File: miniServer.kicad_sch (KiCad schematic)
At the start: 1 part, among them U1 STM32H725VGTx

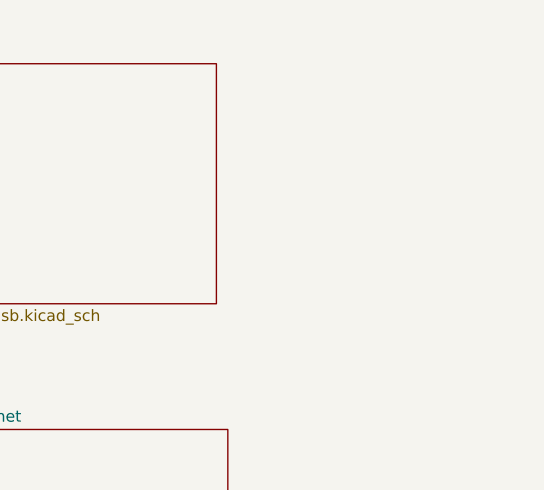
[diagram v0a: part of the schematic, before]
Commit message: Added SDMMC
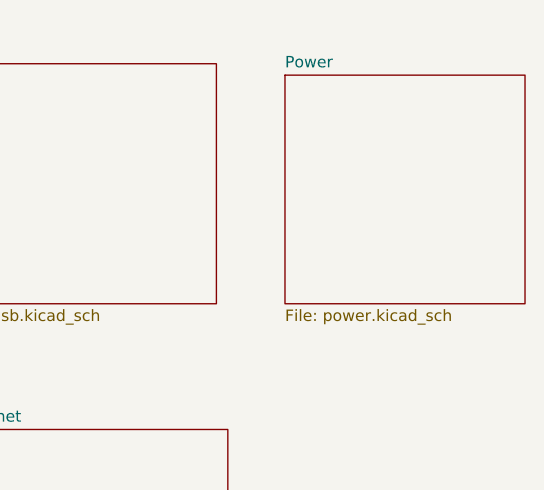
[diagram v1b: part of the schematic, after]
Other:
- added sheet Power (power.kicad_sch)

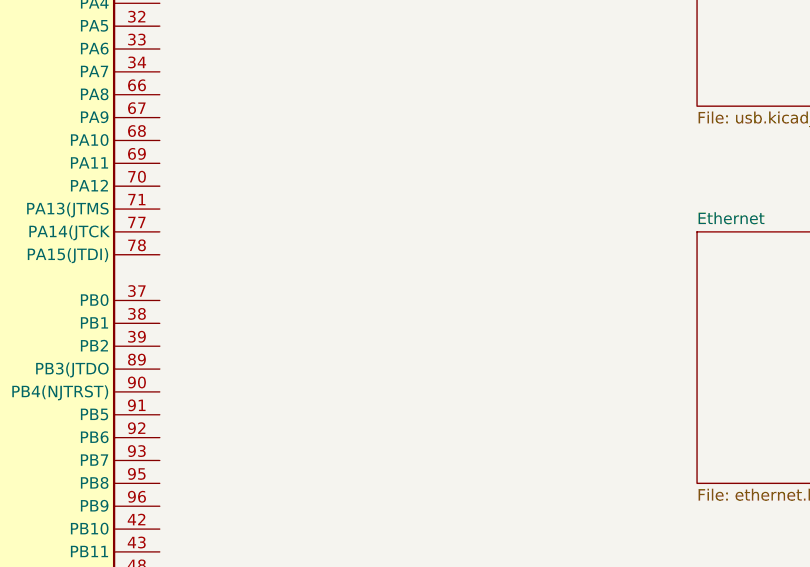
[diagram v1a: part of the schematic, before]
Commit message: Placed some components on PCB layout
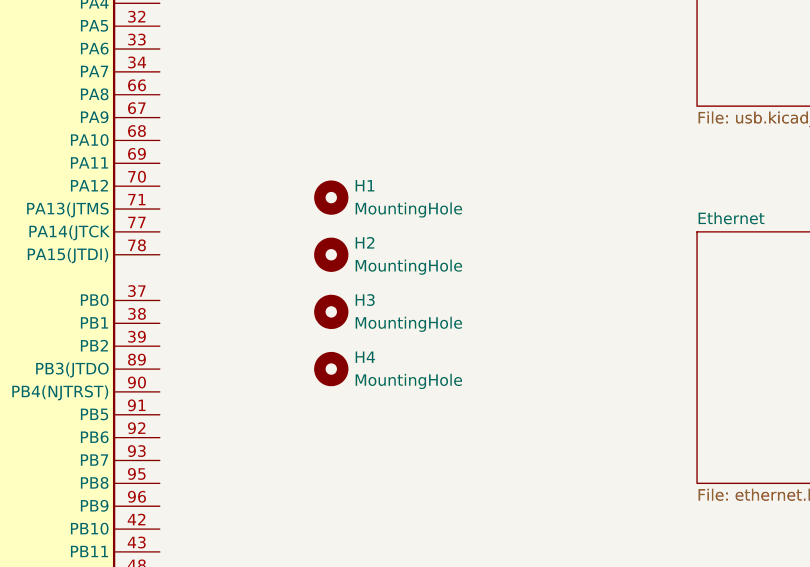
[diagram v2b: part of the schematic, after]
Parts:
- added H1, H2, H3, H4: MountingHole, MountingHole:MountingHole_2.2mm_M2, symbol Mechanical:MountingHole
